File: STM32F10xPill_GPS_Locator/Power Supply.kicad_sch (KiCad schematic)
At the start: 0 parts

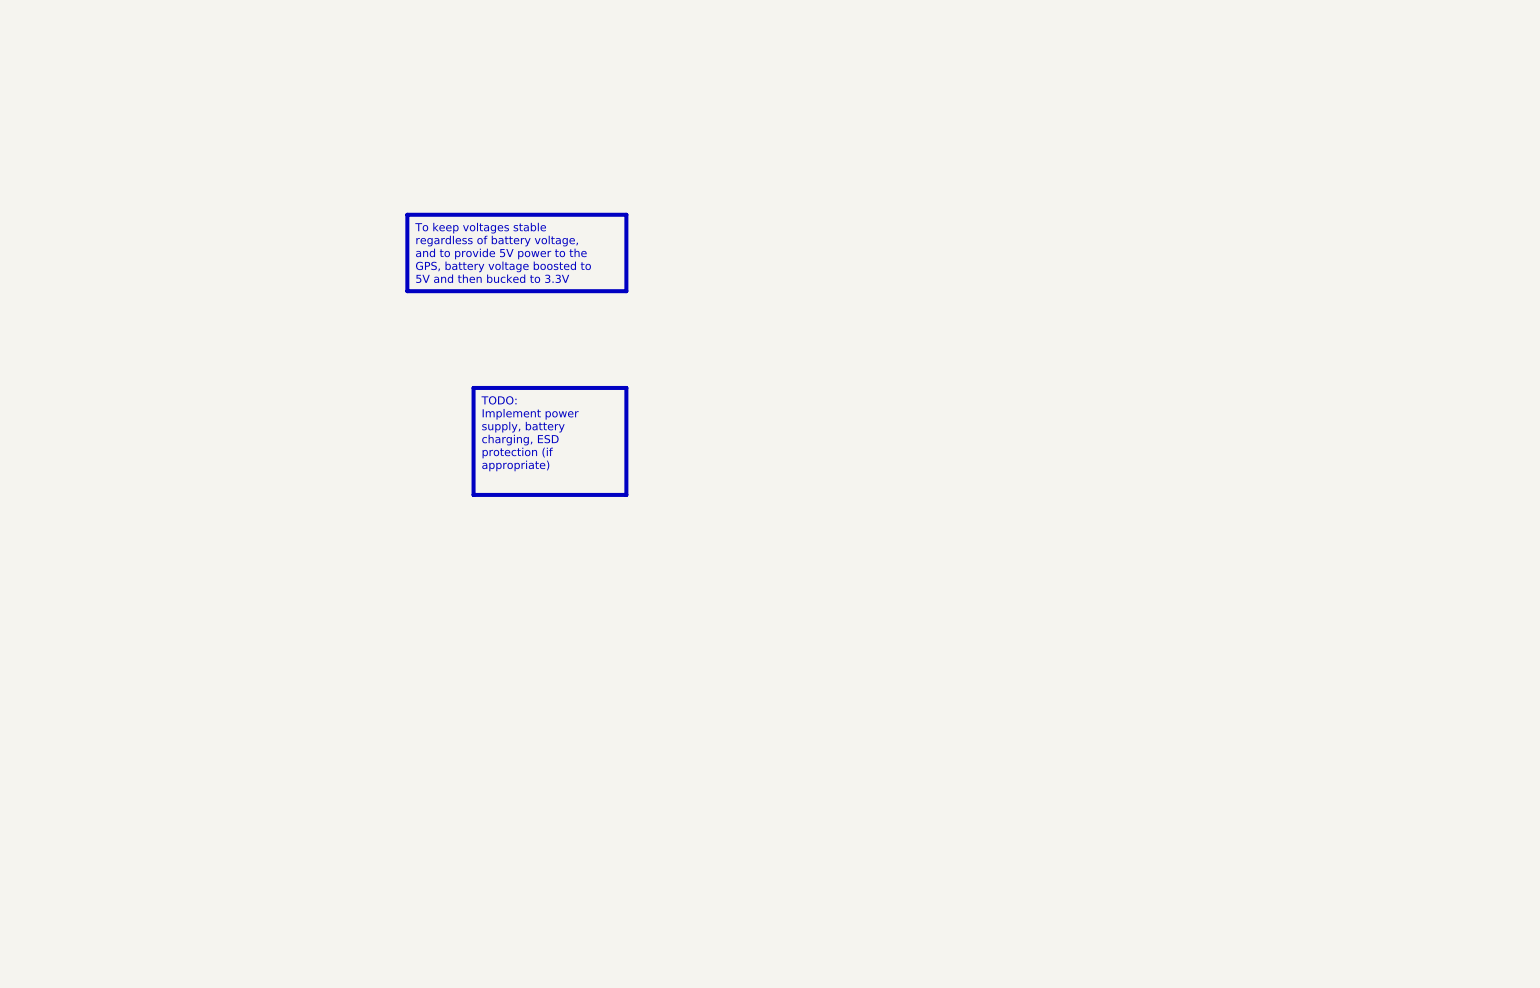
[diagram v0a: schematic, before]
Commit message: Schematic is largely complete
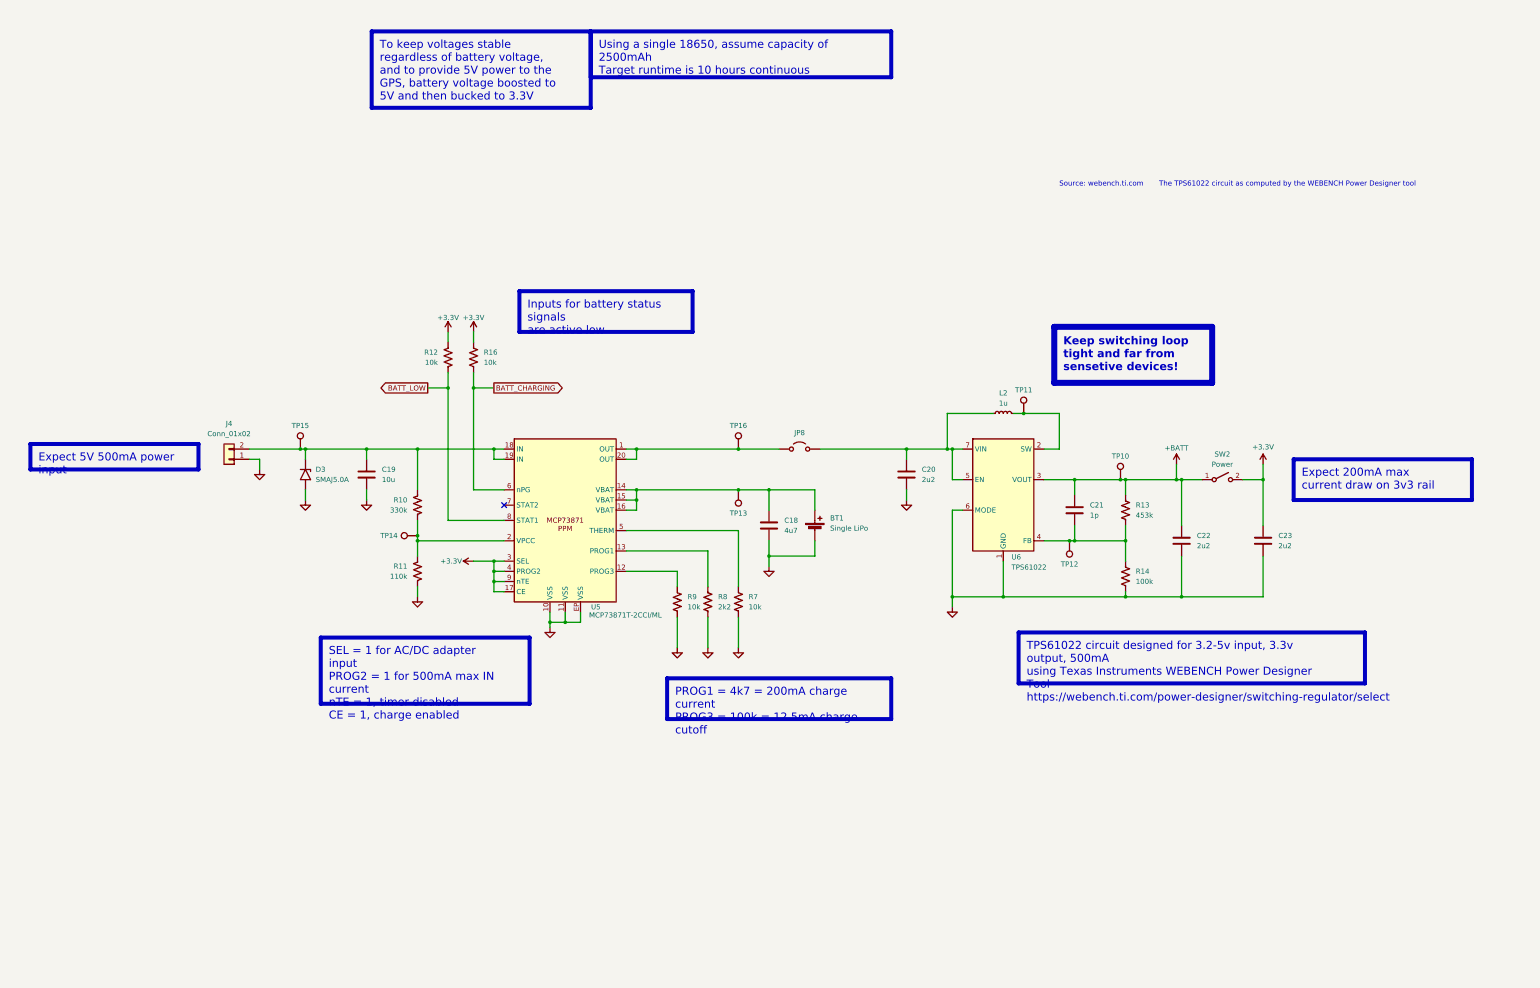
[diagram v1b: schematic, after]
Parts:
- added BT1: Single LiPo, symbol Device:Battery_Cell
- added C18: 4u7, symbol Device:C
- added C19: 10u, symbol Device:C
- added C20, C22, C23: 2u2, symbol Device:C
- added C21: 1p, symbol Device:C
- added D3: SMAJ5.0A, Diode_SMD:D_SMA, symbol Diode:SMAJ5.0A
- added J4: Conn_01x02, symbol Connector_Generic:Conn_01x02
- added JP8: Jumper_2_Open, symbol Jumper:Jumper_2_Open
- added L2: 1u, symbol Device:L_Small
- added R10: 330k, symbol Device:R_US
- added R11: 110k, symbol Device:R_US
- added R12, R16, R7, R9: 10k, symbol Device:R_US
- added R13: 453k, symbol Device:R_US
- added R14: 100k, symbol Device:R_US
- added R8: 2k2, symbol Device:R_US
- added SW2: Power, symbol Switch:SW_SPST
- added TP10, TP11, TP12, TP13, TP14, TP15, TP16: GPS_1PPS, symbol Connector:TestPoint
- added U5: MCP73871T-2CCI/ML, Package_DFN_QFN:QFN-20-1EP_4x4mm_P0.5mm_EP2.5x2.5mm, symbol ICs:MCP73871
- added U6: TPS61022, Package_TO_SOT_SMD:SC-74A-5_1.55x2.9mm_P0.95mm, symbol Converter_DCDC:TPS61022
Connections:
- new net: BT1.1 (+), C18.2, TP13.1, U5.14 (VBAT), U5.15 (VBAT), U5.16 (VBAT)
- new net: C21.1, R13.1, R14.2, TP12.1, U6.4 (FB)
- new net: L2.1, TP11.1, U6.2 (SW)
- new net: C20.2, JP8.2 (B), L2.2, U6.5 (EN), U6.7 (VIN)
- new net: R7.2, U5.5 (THERM)
- new net: R8.2, U5.13 (PROG1)
- new net: R9.2, U5.12 (PROG3)
- new net: C19.2, D3.1 (A1), J4.2 (Pin_2), R10.2, TP15.1, U5.18 (IN), U5.19 (IN)
- new net: R10.1, R11.2, TP14.1, U5.2 (VPCC)
- new net: JP8.1 (A), TP16.1, U5.1 (OUT), U5.20 (OUT)
- new net +3.3V: C23.2, R12.2, R16.2, SW2.2 (B), U5.17 (CE), U5.3 (SEL), U5.4 (PROG2), U5.9 (nTE)
- new net +BATT: C21.2, C22.2, R13.2, SW2.1 (A), TP10.1, U6.3 (VOUT)
- new net BATT_CHARGING: R16.1, U5.6 (nPG)
- new net BATT_LOW: R12.1, U5.8 (STAT1)
- new net GND: BT1.2 (-), C18.1, C19.1, C20.1, C22.1, C23.1, D3.2 (A2), J4.1 (Pin_1), R11.1, R14.1, R7.1, R8.1, R9.1, U5.10 (VSS), U5.11 (VSS), U5.EP (VSS), U6.1 (GND), U6.6 (MODE)
- no-connect marks 0 -> 1
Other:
- note added: "Source: webench.ti.com The TPS61022 circuit as computed by the WEBENCH Power Designer tool"

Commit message: Updated net names, submit schematic for feedback
After feedback is incorporated, PCB layout is ready to begin
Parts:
- added D4, D5: RED, LED_SMD:LED_0603_1608Metric, symbol Device:LED_Filled
- added NT1, NT2: NetTie_2, NetTie:NetTie-2_SMD_Pad0.5mm, symbol Device:NetTie_2
- added R19, R20: 330, Resistor_SMD:R_0402_1005Metric_Pad0.72x0.64mm_HandSolder, symbol Device:R_US
- C18, C19, C20: footprint (none) -> Capacitor_SMD:C_0805_2012Metric
- C21: footprint (none) -> Capacitor_SMD:C_0402_1005Metric
- C22, C23: footprint (none) -> Capacitor_SMD:C_0603_1608Metric
- J4: footprint (none) -> Connector_JST:JST_XH_B2B-XH-A_1x02_P2.50mm_Vertical
- R10, R11, R12, R13, R14, R16, R7, R8, R9: footprint (none) -> Resistor_SMD:R_0402_1005Metric_Pad0.72x0.64mm_HandSolder
- TP10: value GPS_1PPS -> REG_OUT; footprint (none) -> TestPoint:TestPoint_Pad_D1.5mm
- TP11: value GPS_1PPS -> REG_SW; footprint (none) -> TestPoint:TestPoint_Pad_D1.5mm
- TP12: value GPS_1PPS -> REG_FB; footprint (none) -> TestPoint:TestPoint_Pad_D1.5mm
- TP13: value GPS_1PPS -> PPM_BATT; footprint (none) -> TestPoint:TestPoint_Pad_D1.5mm
- TP14: value GPS_1PPS -> PPM_VPCC; footprint (none) -> TestPoint:TestPoint_Pad_D1.5mm
- TP15: value GPS_1PPS -> PPM_IN; footprint (none) -> TestPoint:TestPoint_Pad_D1.5mm
- TP16: value GPS_1PPS -> PPM_OUT; footprint (none) -> TestPoint:TestPoint_Pad_D1.5mm
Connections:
- net +3.3V: now also D4.2 (A), D5.2 (A)
- net BATT_CHARGING: now also R19.1
- net BATT_LOW: now also R20.1
- net PPM_BATT: now reaches BT1.1 (+), C18.2, TP13.1, U5.14 (VBAT), U5.15 (VBAT), U5.16 (VBAT)
- net REG_FB: now reaches C21.1, R13.1, R14.2, TP12.1, U6.4 (FB)
- net REG_SW2: now reaches L2.1, TP11.1, U6.2 (SW)
- net REG_IN: now reaches C20.2, JP8.2 (B), U6.5 (EN)
- net REG_IN: now also NT1.1; no longer L2.2, U6.7 (VIN)
- net PPM_THERM: now reaches R7.2, U5.5 (THERM)
- net PPM_PROG1: now reaches R8.2, U5.13 (PROG1)
- net PPM_PROG3: now reaches R9.2, U5.12 (PROG3)
- net 5V_IN: now reaches C19.2, D3.1 (A1), J4.2 (Pin_2), TP15.1
- net 5V_IN: now also NT2.1; no longer R10.2, U5.18 (IN), U5.19 (IN)
- net PPM_VPCC: now reaches R10.1, R11.2, TP14.1, U5.2 (VPCC)
- net PPM_OUT: now reaches JP8.1 (A), TP16.1, U5.1 (OUT), U5.20 (OUT)
- new net: D5.1 (K), R20.2
- new net: D4.1 (K), R19.2
- new net PPM_IN: NT2.2, R10.2, U5.18 (IN), U5.19 (IN)
- new net REG_SW1: L2.2, NT1.2, U6.7 (VIN)
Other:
- moved on the sheet: C20, L2, R12, R16

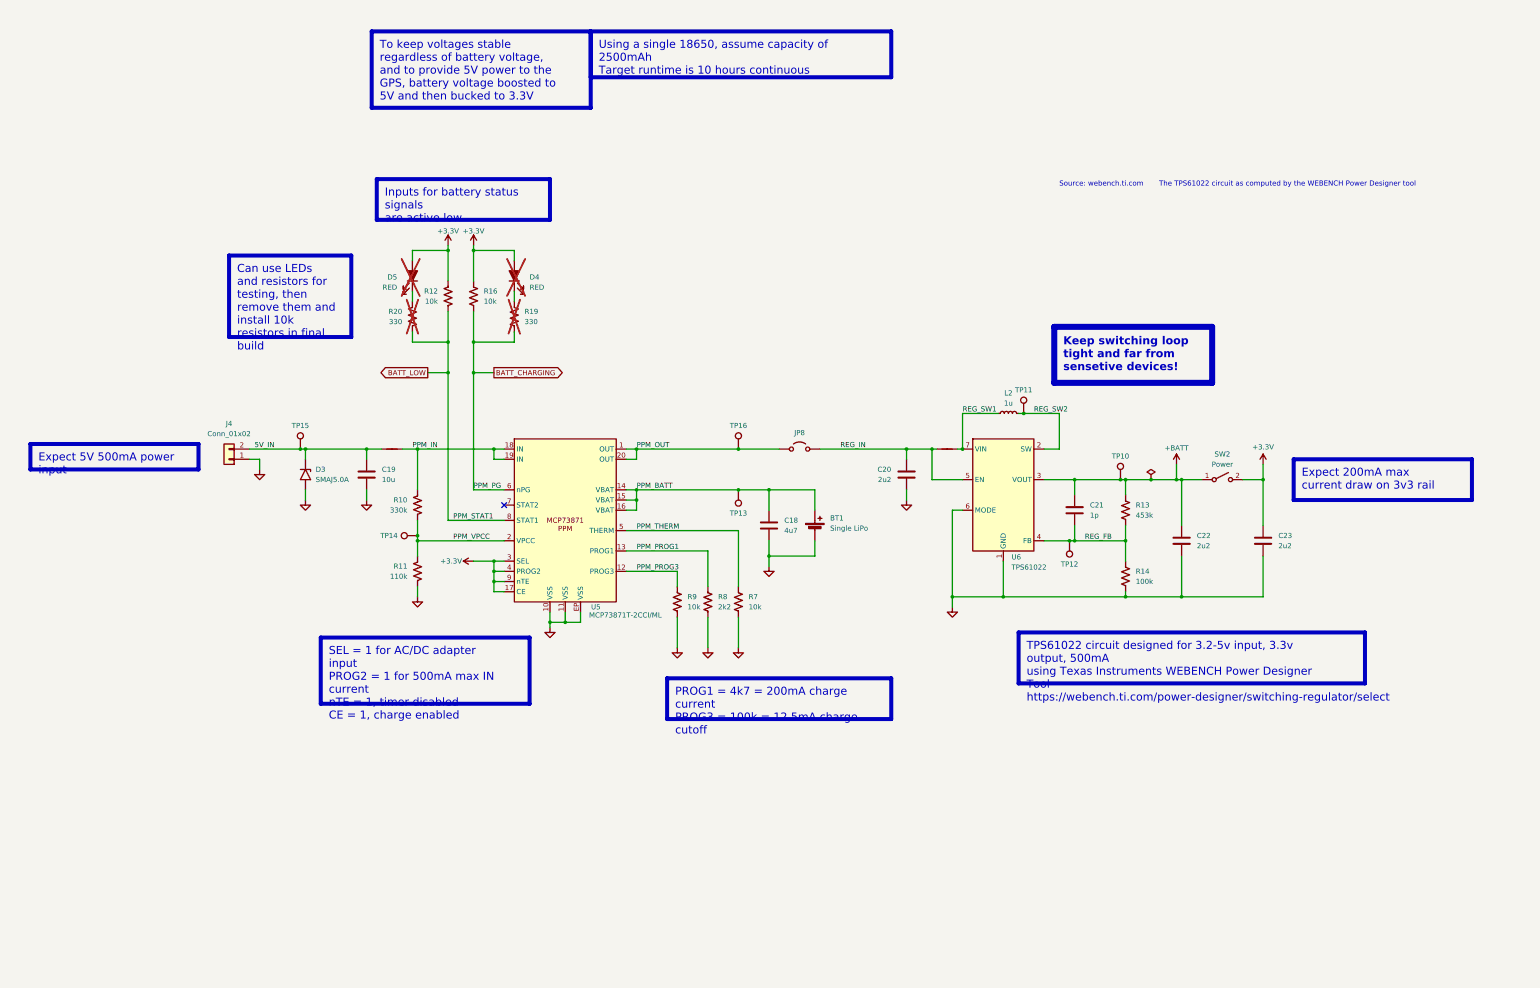
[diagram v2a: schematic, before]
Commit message: Add all footprints and symbols, retouch schametic
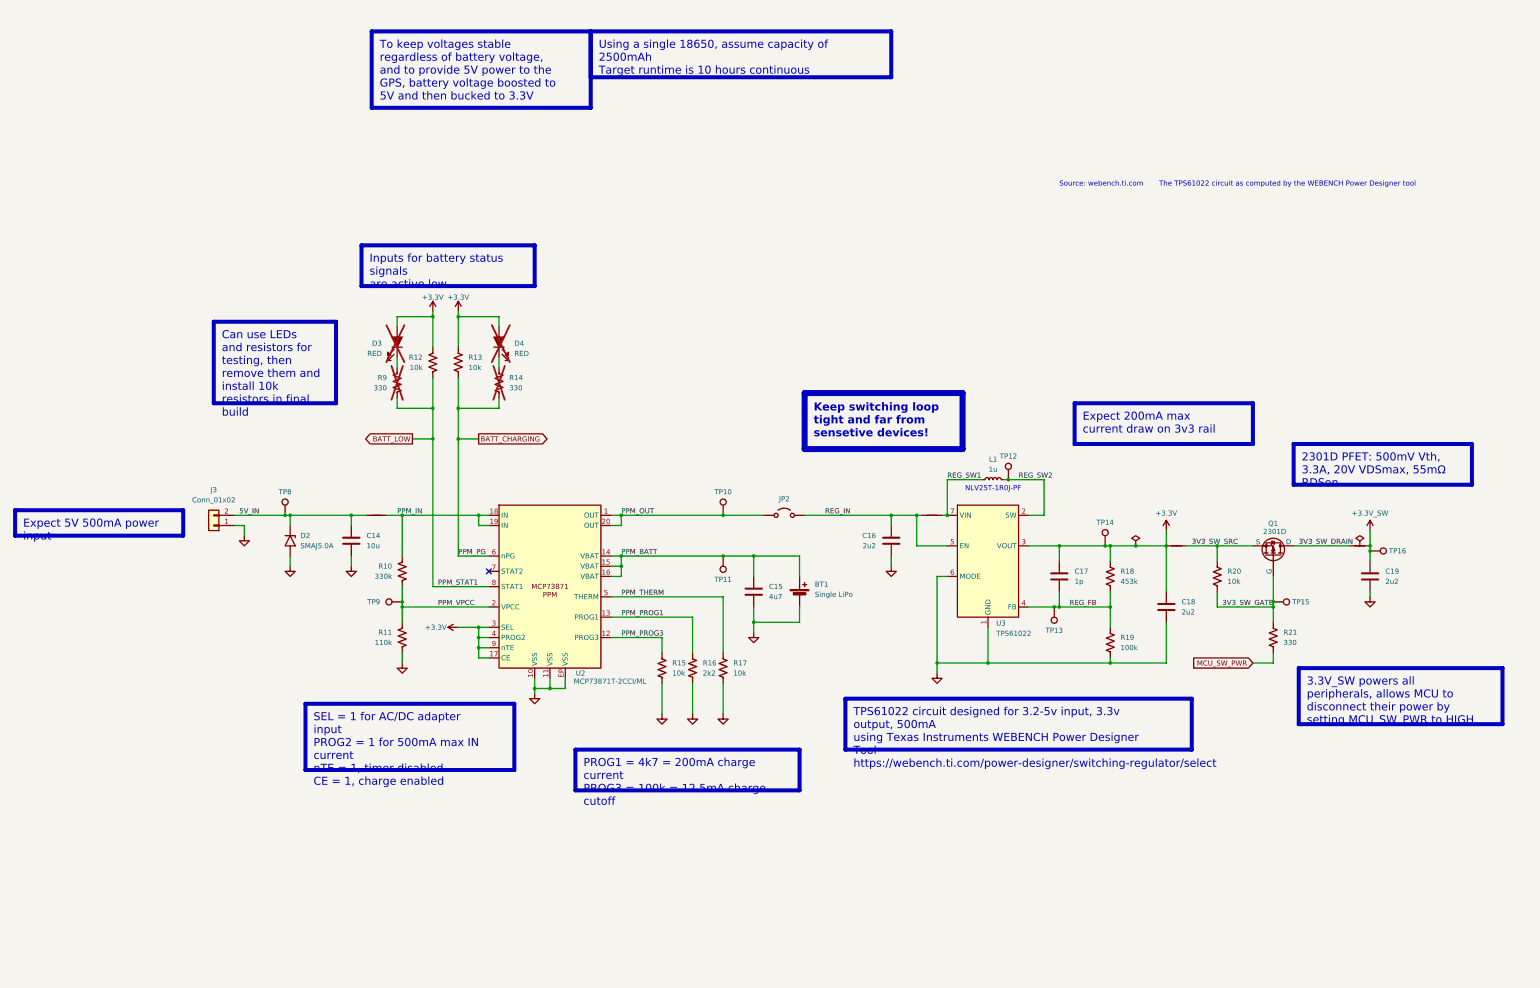
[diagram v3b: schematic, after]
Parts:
- removed C23: 2u2, Capacitor_SMD:C_0603_1608Metric, symbol Device:C
- removed SW2: Power, symbol Switch:SW_SPST
- added C19: 2u2, Capacitor_SMD:C_0603_1608Metric, symbol Device:C
- added NT3, NT4: NetTie_2, NetTie:NetTie-2_SMD_Pad0.5mm, symbol Device:NetTie_2
- added Q1: 2301D, Package_TO_SOT_SMD:SOT-23, symbol Simulation_SPICE:PMOS
- added R20: 10k, Resistor_SMD:R_0402_1005Metric_Pad0.72x0.64mm_HandSolder, symbol Device:R_US
- added R21: 330, Resistor_SMD:R_0402_1005Metric_Pad0.72x0.64mm_HandSolder, symbol Device:R_US
- added TP15: 3V3_SW_GATE, TestPoint:TestPoint_Pad_D1.5mm, symbol Connector:TestPoint
- added TP16: 3V3_SW, TestPoint:TestPoint_Pad_D1.5mm, symbol Connector:TestPoint
- BT1: footprint (none) -> Battery:BatteryHolder_MPD_BH-18650-PC2
- JP2: renamed from JP8; footprint (none) -> Jumper:SolderJumper-2_P1.3mm_Open_Pad1.0x1.5mm
- L1: renamed from L2; footprint (none) -> Inductor_SMD:L_1008_2520Metric; LCSC Part (none) -> C76827
- renumbered C19 to C14, C18 to C15, C20 to C16, C21 to C17, C22 to C18, D3 to D2, D5 to D3, J4 to J3, NT2 to NT1, NT1 to NT2, R16 to R13, R19 to R14, R9 to R15, R8 to R16, R7 to R17, R13 to R18, R14 to R19, R20 to R9, TP16 to TP10, TP13 to TP11, TP11 to TP12, TP12 to TP13, TP10 to TP14, TP15 to TP8, TP14 to TP9, U5 to U2, U6 to U3
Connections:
- net +BATT is gone; now on net +3.3V: C17.2, C18.2, R18.2, TP14.1, U3.3 (VOUT)
- net +3.3V: now also NT3.1
- net GND: now also C19.1
- new net +3.3V_SW: C19.2, NT4.2, TP16.1
- new net 3V3_SW_DRAIN: NT4.1, Q1.1 (D)
- new net 3V3_SW_GATE: Q1.2 (G), R20.1, R21.2, TP15.1
- new net 3V3_SW_SRC: NT3.2, Q1.3 (S), R20.2
- new net MCU_SW_PWR: R21.1
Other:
- note added: "NLV25T-1R0J-PF"
- moved on the sheet: BT1, C14, C15, C16, C17, C18, D2, D3, D4, J3, JP2, L1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

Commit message: Begin PCB layout
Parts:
- J3: footprint Connector_JST:JST_XH_B2B-XH-A_1x02_P2.50mm_Vertical -> Connector_JST:JST_PH_B2B-PH-K_1x02_P2.00mm_Vertical
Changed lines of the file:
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@@
 			"K1enO1oAACA7INtoeQAAAAAAAAAAAAAAAAAAAAAAADH4V80+WgAAduEVQpVo38HRxks+OgMWQiqr"
 			"3cFnOVU+WPIVQuCJ3sEcgFA+AgAAAFhW0ac7WgAAAAAAAAAAAAAAAAAAAAAAADADkGM7WgAAul7l"
-			"Ps8iqT4AAAAAAAAAAEAX4W47WgAAoQMAAAAAAA=="
+			"Ps8iqT4AAAAAAAAAAEAX4W47WgAAoQMAAAAAAGhhbmRsZShEMC54KSwgMkQ7Ck1BWC5GIFIxLngs"
+			"IFIwLCBSMC55OwpNSU4uRiBSMC54LCBSMCwgUjAueTsKTUlOLkYgUjAueiwgUjAsIFIxLng7Ck1B"
+			"RC5GMzIgUjAudywgLVIxLnksIHswLjI1LCAwLjUsIDAsIDB9LngsIHswLjI1LCAwLjUsIDAsIDB9"
+			"Lnk7Ck1BRC5GMzIgUjEueCwgUjEueSwgezAuMjUsIDAsIDAsIDB9LCAtUjAudzsKTUFYLkYgUjAu"
+			"eCwgUjAsIFIwLno7CkFERC5GMzIgUjAueSwgUjEueCwgezAuNSwgMCwgMCwgMH0ueDsKQURELkYz"
+			"MiBSMC54LCBSMCwgLVIwLnc7CkRJVi5GMzIuU0FUIFIwLngsIFIwLCBSMC55OwpNQUQuRjMyIFIw"
+			"LnksIC1SMC54LCB7MiwgMywgMCwgMH0ueCwgezIsIDMsIDAsIDB9OwpNVUwuRjMyIFIwLngsIFIw"
+			"LCBSMDsKTVVMLkYzMiBSMC54LCBSMCwgUjAueTsKTVVMLkYzMiByZXN1bHRfY29sb3IwLncsIGZy"
+			"YWdtZW50LmNvbG9yLCBSMC54OwpNT1YuRiByZXN1bHRfY29sb3IwLnh5eiwgZnJhZ21lbnQuY29s"
+			"b3I7CkVMU0U7Ck1PVi5GIHJlc3VsdF9jb2xvcjAsIGZyYWdtZW50LmNvbG9yOwpFTkRJRjsKRU5E"
+			"SUY7CkVORElGOwpFTkRJRjsKRU5ECggAAAAAAAAAAAAAAAAAAAAAAAAAAAAAAAAAAAAAAAAAAAAA"
+			"AAAAAAAAAAAAAAAAAAAAAAAAAAAAAAAAAAAAAAAAAAAAAAAAAAAAAAAAAAAAAAAAAAAAAAAAAAAA"
+			"AAAAAAAAAAAAAAAAAAAAAAAAAAAAAAAAAAAAAAAAAAAAAAAAAAAAAAAAAAABAAAAIAAAAAEAAAAA"
+			"/////////////////////////////////////////wAAAAAAAAAAAAAAAAAAAAAAAAAAAAAAAAAA"
+			"AAAAAAAAAAAAAAAAAAAAAAAAAAAAAAAAAAAAAAAAAAAAAAAAAAAAAAAAAAAAAAAAAAAAAAAAAAAA"
+			"AAAAAAAAAAAAAAAAAAEAAAAAAAAAAAAAAAAAAAAAAAAAAAAAAAAAAAAAAAAAAAAAAAAAAAD/////"
+			"/////wAAAAAAAAAAAAAAAAAAAAAAAAAAAAAAAAAAAAAAAQAAALEAAAAAAAAAcGsoZztaAADAOyDb"
+			"aHkAAEBhDHo7WgAAIDsg22h5AAAAAAAAAAAAAAAAAAD9AAAAAAAAAAEAAAAwn4F2O1oAAMCGAAAA"
+			"AAAAIAAAAAAAAAAp0Y3TPloAAAAAAAAAAAAAsA=="
 		)
 	)
@@
 			)
 		)
-		(property "Footprint" "Connector_JST:JST_XH_B2B-XH-A_1x02_P2.50mm_Vertical"
+		(property "Footprint" "Connector_JST:JST_PH_B2B-PH-K_1x02_P2.00mm_Vertical"
 			(at 76.2 152.4 0)
 			(effects

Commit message: Initial placement completed
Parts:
- U3: value TPS61022 -> TPS61022RWUR; footprint Package_TO_SOT_SMD:SC-74A-5_1.55x2.9mm_P0.95mm -> Package_DFN_QFN:Texas_RWU0007A_VQFN-7_2x2mm_P0.5mm; LCSC Part (none) -> C915088
- renumbered C14 to C15, C15 to C16, C16 to C17, C17 to C18, C18 to C19, C19 to C20, R9 to R10, R10 to R11, R11 to R12, R12 to R13, R13 to R14, R14 to R15, R15 to R16, R16 to R17, R17 to R18, R18 to R19, R19 to R20, R20 to R21, R21 to R22, TP14 to TP10, TP15 to TP11, TP16 to TP12, TP8 to TP4, TP9 to TP5, TP10 to TP6, TP11 to TP7, TP12 to TP8, TP13 to TP9
